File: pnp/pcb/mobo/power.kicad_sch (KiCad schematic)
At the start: 31 parts, among them J12 COMBO_POWER_JACK, U11 FDS4435BZ, U12 TPS54331, U13 AP1117-33, U6 Fuse_Holder_3568

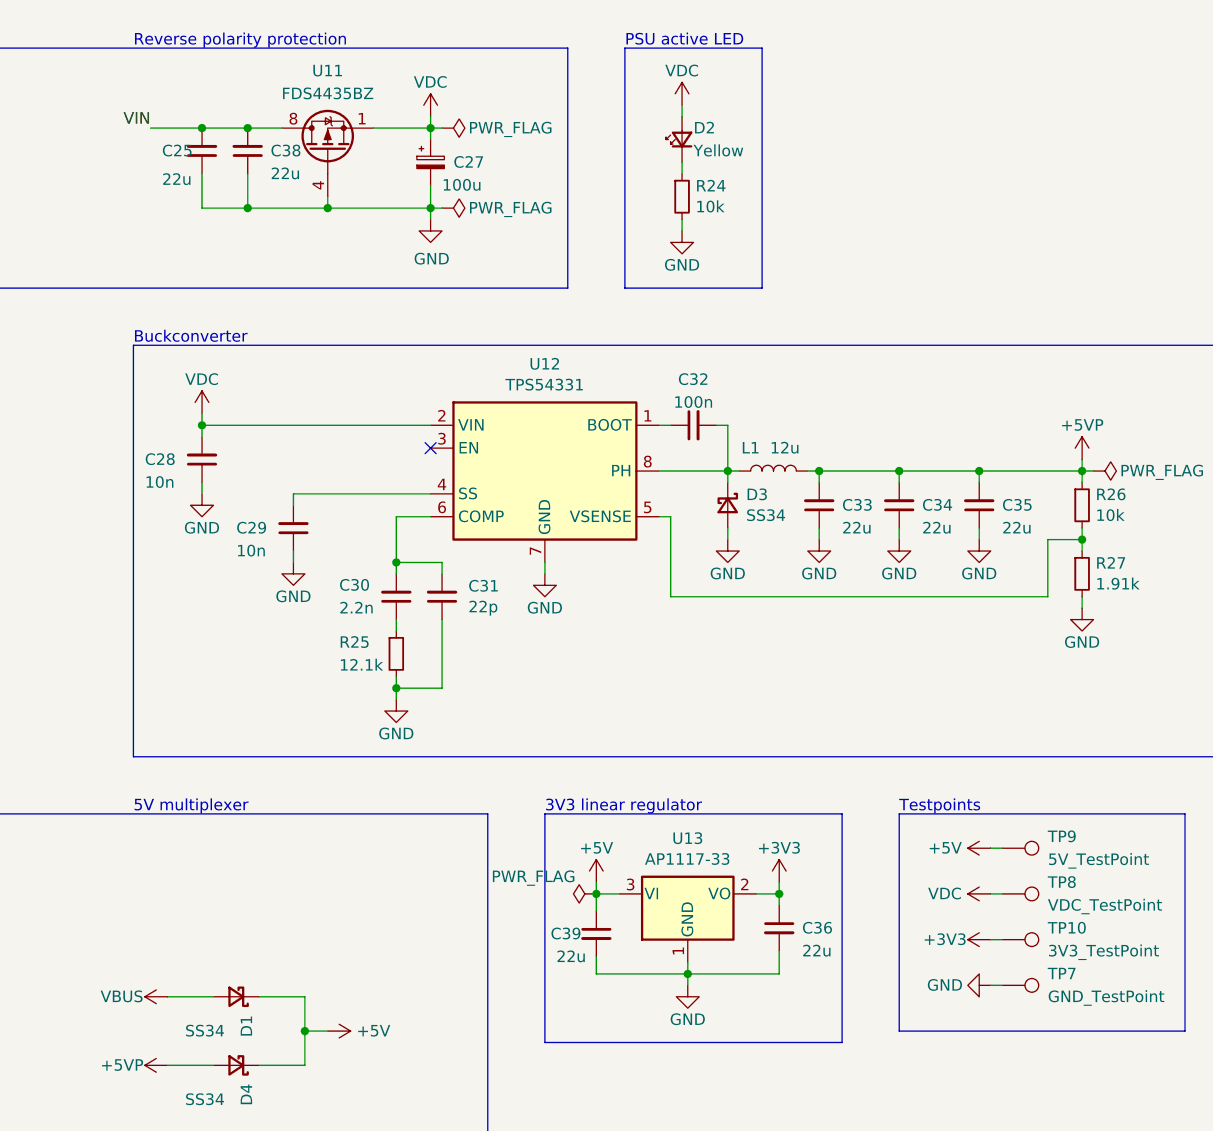
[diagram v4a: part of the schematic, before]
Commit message: replaces SRL05 for SRV05 due to pricing and availability, routed mostfet gate resistors and added 2g34 buffer to boost the voltage of the servo drive pins. consolidated a random cap value that could be switched to an existing one.
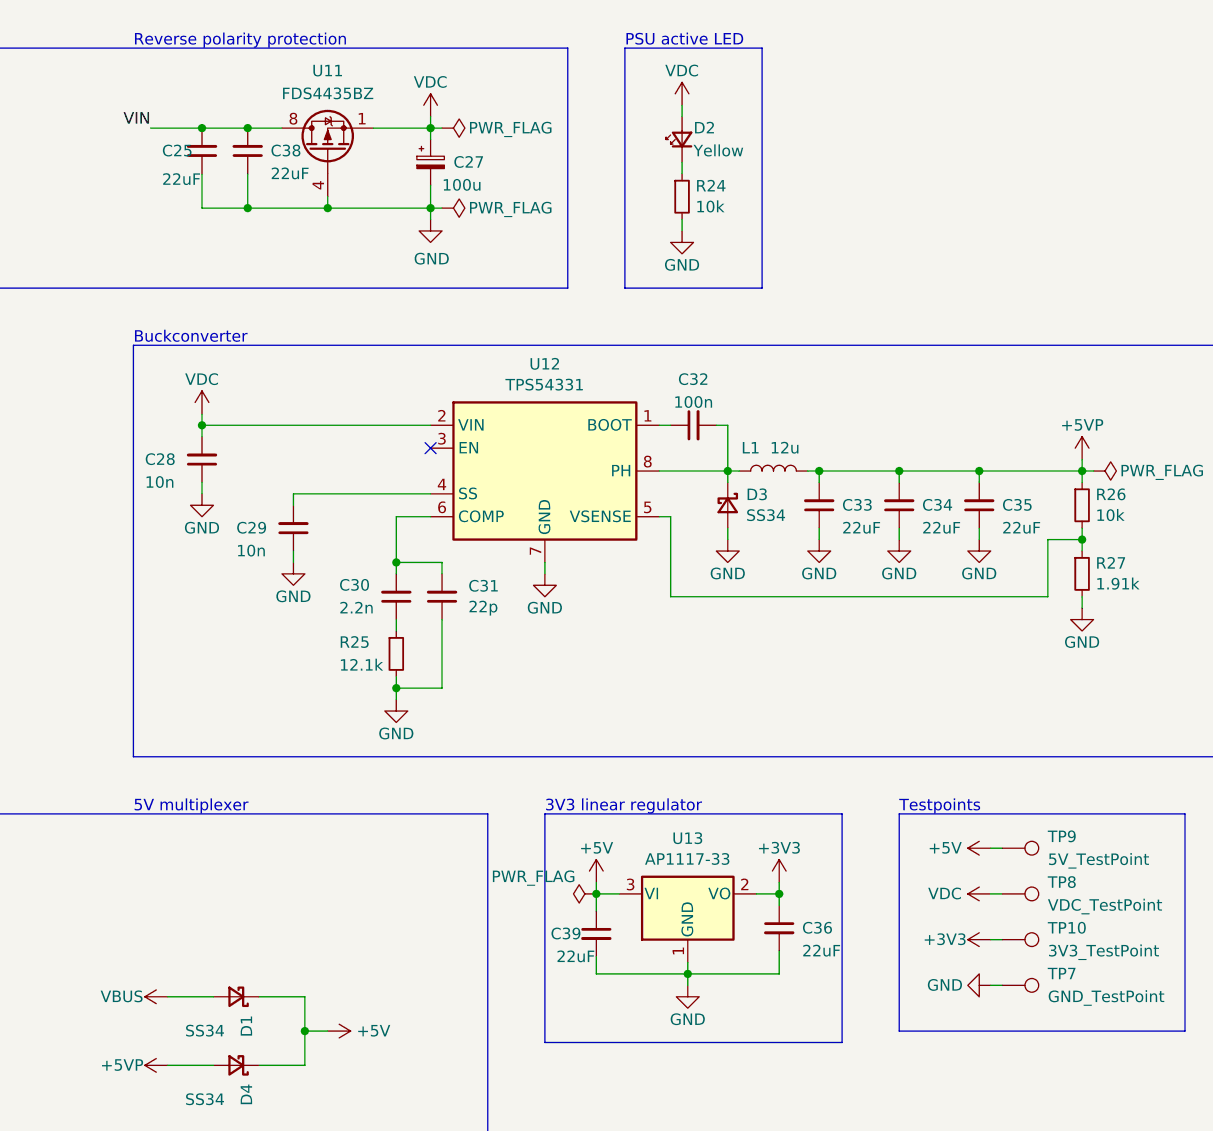
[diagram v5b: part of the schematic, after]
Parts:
- C25, C33, C34, C35, C36, C38, C39: value 22u -> 22uF
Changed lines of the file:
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@@
       (effects (font (size 1.27 1.27)) (justify left))
     )
-    (property "Value" "22u" (id 1) (at 163.195 147.32 0)
+    (property "Value" "22uF" (id 1) (at 163.195 147.32 0)
       (effects (font (size 1.27 1.27)) (justify left))
     )
@@
       (effects (font (size 1.27 1.27)) (justify right))
     )
-    (property "Value" "22u" (id 1) (at 185.42 100.33 0)
+    (property "Value" "22uF" (id 1) (at 185.42 100.33 0)
       (effects (font (size 1.27 1.27)) (justify right))
     )
@@
       (effects (font (size 1.27 1.27)) (justify right))
     )
-    (property "Value" "22u" (id 1) (at 176.53 100.33 0)
+    (property "Value" "22uF" (id 1) (at 176.53 100.33 0)
       (effects (font (size 1.27 1.27)) (justify right))
     )
@@
       (effects (font (size 1.27 1.27)) (justify right))
     )
-    (property "Value" "22u" (id 1) (at 167.64 100.33 0)
+    (property "Value" "22uF" (id 1) (at 167.64 100.33 0)
       (effects (font (size 1.27 1.27)) (justify right))
     )
@@
       (effects (font (size 1.27 1.27)) (justify right))
     )
-    (property "Value" "22u" (id 1) (at 92.075 61.595 0)
+    (property "Value" "22uF" (id 1) (at 92.075 61.595 0)
       (effects (font (size 1.27 1.27)) (justify right))
     )
@@
       (effects (font (size 1.27 1.27)) (justify left))
     )
-    (property "Value" "22u" (id 1) (at 135.89 147.955 0)
+    (property "Value" "22uF" (id 1) (at 135.89 147.955 0)
       (effects (font (size 1.27 1.27)) (justify left))
     )
@@
       (effects (font (size 1.27 1.27)) (justify right))
     )
-    (property "Value" "22u" (id 1) (at 104.14 60.96 0)
-      (effects (font (size 1.27 1.27)) (justify right))
-    )
+    (property "Value" "22uF" (id 1) (at 104.14 60.96 0)
+      (effects (font (size 1.27 1.27)) (justify right))
+    )

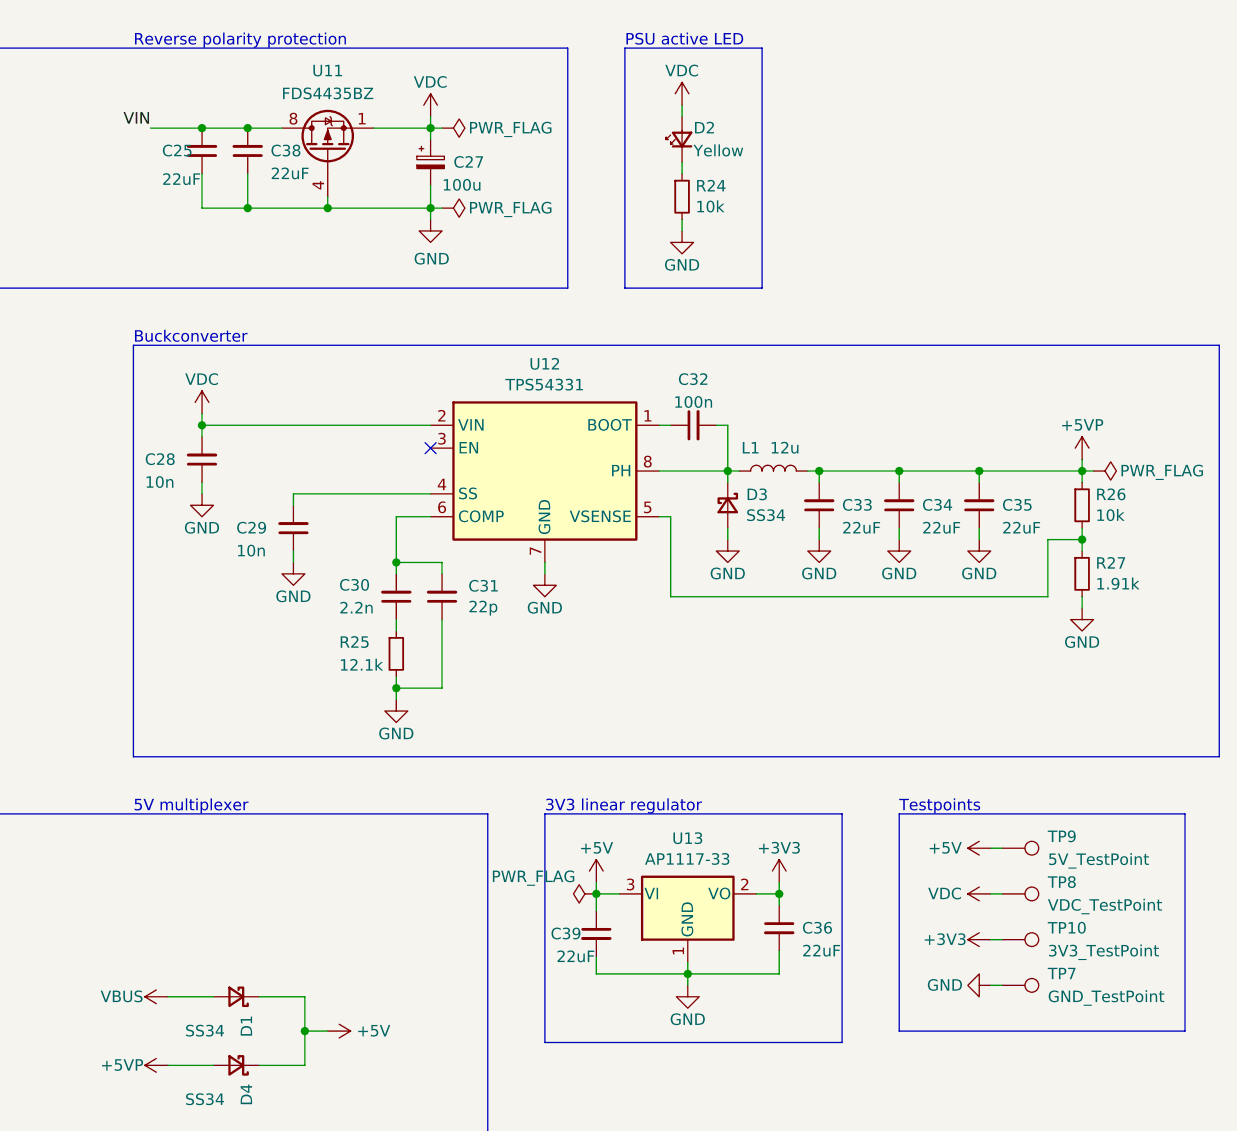
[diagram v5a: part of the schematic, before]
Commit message: Update mobo schematic with part numbers and ratings
All parts now have part numbers for at least one reseller or manufacturer along with rating specifications.

Note: I did not update the PCB with these new properties, as it seems the PCB is a bit out of sync with the schematic.
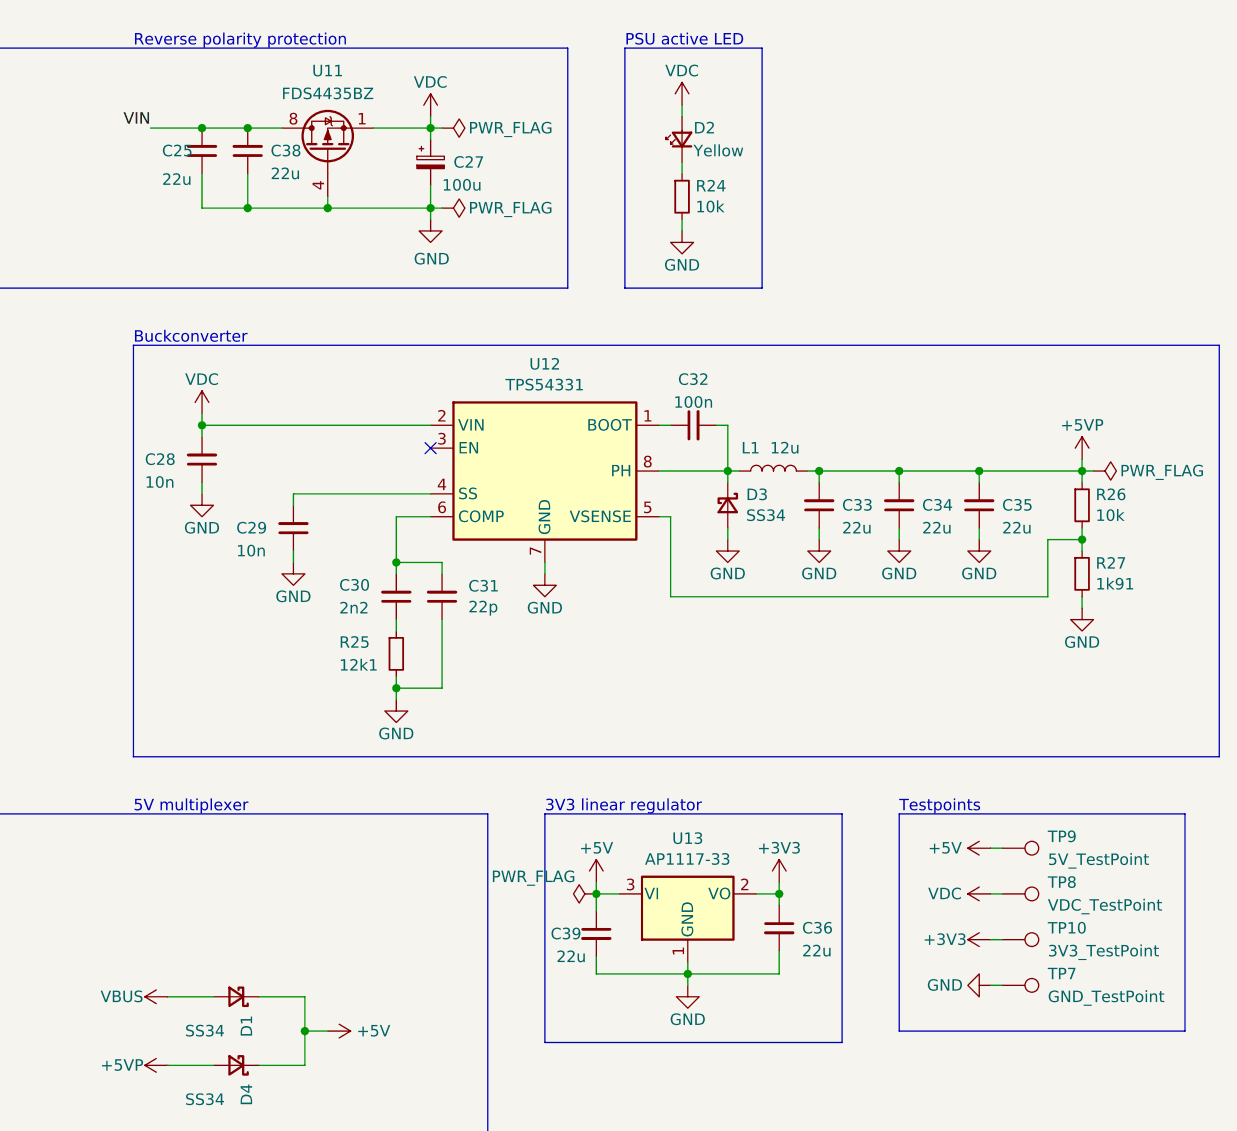
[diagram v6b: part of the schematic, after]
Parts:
- C25, C33, C34, C35, C38: value 22uF -> 22u; Notes (none) -> 25V/20%
- C27: Notes (none) -> 35V/20%/Aluminum
- C28, C29, C32: Notes (none) -> 50V/10%
- C30: value 2.2n -> 2n2; Notes (none) -> 50V/10%
- C31: Notes (none) -> 50V/5%
- C36, C39: value 22uF -> 22u; Notes (none) -> 50V/10%
- D1, D3, D4: Notes Vf<=0.55V,I>=2A,Vr>=24V -> 40V/3A
- D2: Notes (none) -> 20mA
- J12: Digikey (none) -> CP-102A-ND
- R24: Notes (none) -> 125mW/1%
- R25: value 12.1k -> 12k1; Notes 1% -> 125mW/1%
- R26: Notes 1% -> 125mW/1%
- R27: value 1.91k -> 1k91; Notes (none) -> 125mW/1%
- U11: Notes (none) -> 30V/8A
- U6: Digikey (none) -> 36-3568-ND
